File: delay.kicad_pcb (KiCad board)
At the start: 2 copper layers, 0 parts

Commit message: add remaining footprints, start pcb design process
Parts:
- added C1: 10uF, Capacitor:EEE1AA220WR, F.Cu at (89.2, 130.9)
- added C10: 1uF, Capacitor_SMD:C_0805_2012Metric_Pad1.18x1.45mm_HandSolder, F.Cu at (227.4, 80.6)
- added C11: 22nF, Capacitor_SMD:C_0805_2012Metric_Pad1.18x1.45mm_HandSolder, F.Cu at (250.2, 66.2)
- added C12: 2n2, Capacitor_SMD:C_0805_2012Metric_Pad1.18x1.45mm_HandSolder, F.Cu at (232.2, 65.6)
- added C13: 47uF, Capacitor:EEE1AA101SP, F.Cu at (253.5, 74.1)
- added C14: 2n2, Capacitor_SMD:C_0805_2012Metric_Pad1.18x1.45mm_HandSolder, F.Cu at (232.2, 68.6)
- added C15: 47nF, Capacitor_SMD:C_0805_2012Metric_Pad1.18x1.45mm_HandSolder, F.Cu at (232.2, 71.6)
- added C16: 100nF, Capacitor_SMD:C_0805_2012Metric_Pad1.18x1.45mm_HandSolder, F.Cu at (232.2, 74.6)
- added C17: 10nF, Capacitor_SMD:C_0805_2012Metric_Pad1.18x1.45mm_HandSolder, F.Cu at (232.2, 77.6)
- added C18: 15nF, Capacitor_SMD:C_0805_2012Metric_Pad1.18x1.45mm_HandSolder, F.Cu at (232.2, 80.6)
- added C19: 100nF, Capacitor_SMD:C_0805_2012Metric_Pad1.18x1.45mm_HandSolder, F.Cu at (255.3, 66.2)
- added C2: 100uF, Capacitor:EEE1AA101SP, F.Cu at (78.7, 132.1)
- added C20: 1uF, Capacitor_SMD:C_0805_2012Metric_Pad1.18x1.45mm_HandSolder, F.Cu at (237.0, 65.6)
- added C21: 100nF, Capacitor_SMD:C_0805_2012Metric_Pad1.18x1.45mm_HandSolder, F.Cu at (237.0, 68.6)
- added C22: 100nF, Capacitor_SMD:C_0805_2012Metric_Pad1.18x1.45mm_HandSolder, F.Cu at (237.0, 71.6)
- added C23: 1uF, Capacitor_SMD:C_0805_2012Metric_Pad1.18x1.45mm_HandSolder, F.Cu at (237.0, 74.6)
- added C3: 10uF, Capacitor:EEE1AA220WR, F.Cu at (89.2, 138.3)
- added C4: 100nF, Capacitor_SMD:C_0805_2012Metric_Pad1.18x1.45mm_HandSolder, F.Cu at (74.7, 124.5)
- added C5: 1uF, Capacitor_SMD:C_0805_2012Metric_Pad1.18x1.45mm_HandSolder, F.Cu at (161.1, 88.9)
- added C6: 22nF, Capacitor_SMD:C_0805_2012Metric_Pad1.18x1.45mm_HandSolder, F.Cu at (146.0, 86.9)
- added C7: 47pF, Capacitor_SMD:C_0805_2012Metric_Pad1.18x1.45mm_HandSolder, F.Cu at (150.9, 86.8)
- added C8: 100pF, Capacitor_SMD:C_0805_2012Metric_Pad1.18x1.45mm_HandSolder, F.Cu at (163.6, 76.2)
- added C9: 4n7, Capacitor_SMD:C_0805_2012Metric_Pad1.18x1.45mm_HandSolder, F.Cu at (227.4, 77.6)
- added D1: 1N4001, Diodes:DIOM5226X240N, F.Cu at (73.7, 144.8)
- added D2: LED, Diodes:TB00150002BE, F.Cu at (167.6, 132.1)
- added DELAY1: 50kB, Potentiometer_THT:Potentiometer_Alps_RK163_Single_Horizontal, F.Cu at (142.2, 40.6)
- added FDBK1: 50kB, Potentiometer_THT:Potentiometer_Alps_RK163_Single_Horizontal, F.Cu at (167.5, 40.6)
- added J1: Footswitch_Terminal_01x02, Terminal:TB00150002BE, F.Cu at (154.9, 144.8)
- added J2: LED_Socket_01x02, Diodes:TB00150002BE, F.Cu at (167.0, 144.8)
- added J3: Footswitch_Terminal_Signal_01x02, Terminal:TB00150002BE, F.Cu at (180.3, 144.8)
- added J4: Power_Supply_Terminal_01x02, Terminal:TB00150002BE, F.Cu at (210.7, 45.7)
- added J5: IO_Ground_Terminal_01x02, Terminal:TB00150002BE, F.Cu at (226.1, 45.7)
- added MIX1: 50kB, Potentiometer_THT:Potentiometer_Alps_RK163_Single_Horizontal, F.Cu at (192.9, 40.6)
- added R1: 33, Resistor_SMD:R_0805_2012Metric_Pad1.20x1.40mm_HandSolder, F.Cu at (82.3, 121.5)
- added R10: 10k, Resistor_SMD:R_0805_2012Metric_Pad1.20x1.40mm_HandSolder, F.Cu at (189.3, 71.1)
- added R11: 10k, Resistor_SMD:R_0805_2012Metric_Pad1.20x1.40mm_HandSolder, F.Cu at (189.5, 74.7)
- added R12: 5k1, Resistor_SMD:R_0805_2012Metric_Pad1.20x1.40mm_HandSolder, F.Cu at (189.5, 77.6)
- added R13: 10k, Resistor_SMD:R_0805_2012Metric_Pad1.20x1.40mm_HandSolder, F.Cu at (189.5, 80.6)
- added R14: 20k, Resistor_SMD:R_0805_2012Metric_Pad1.20x1.40mm_HandSolder, F.Cu at (189.5, 83.5)
- added R15: 2k7, Resistor_SMD:R_0805_2012Metric_Pad1.20x1.40mm_HandSolder, F.Cu at (199.7, 70.7)
- added R16: 10k, Resistor_SMD:R_0805_2012Metric_Pad1.20x1.40mm_HandSolder, F.Cu at (199.7, 73.7)
- added R17: 1k, Resistor_SMD:R_0805_2012Metric_Pad1.20x1.40mm_HandSolder, F.Cu at (194.0, 71.1)
- added R18: 10k, Resistor_SMD:R_0805_2012Metric_Pad1.20x1.40mm_HandSolder, F.Cu at (194.2, 74.7)
- added R19: 2k, Resistor_SMD:R_0805_2012Metric_Pad1.20x1.40mm_HandSolder, F.Cu at (194.2, 77.6)
- added R2: 10k, Resistor_SMD:R_0805_2012Metric_Pad1.20x1.40mm_HandSolder, F.Cu at (82.3, 124.5)
- added R20: 20k, Resistor_SMD:R_0805_2012Metric_Pad1.20x1.40mm_HandSolder, F.Cu at (163.6, 86.4)
- added R21: 4k7, Resistor_SMD:R_0805_2012Metric_Pad1.20x1.40mm_HandSolder, F.Cu at (166.6, 121.9)
- added R3: 10k, Resistor_SMD:R_0805_2012Metric_Pad1.20x1.40mm_HandSolder, F.Cu at (74.7, 139.7)
- added R4: 1k, Resistor_SMD:R_0805_2012Metric_Pad1.20x1.40mm_HandSolder, F.Cu at (166.6, 88.9)
- added R5: 22k, Resistor_SMD:R_0805_2012Metric_Pad1.20x1.40mm_HandSolder, F.Cu at (161.0, 91.4)
- added R6: 180k, Resistor_SMD:R_0805_2012Metric_Pad1.20x1.40mm_HandSolder, F.Cu at (146.3, 91.4)
- added R7: 1M, Resistor_SMD:R_0805_2012Metric_Pad1.20x1.40mm_HandSolder, F.Cu at (146.3, 94.4)
- added R8: 12k, Resistor_SMD:R_0805_2012Metric_Pad1.20x1.40mm_HandSolder, F.Cu at (163.6, 81.3)
- added R9: 360k, Resistor_SMD:R_0805_2012Metric_Pad1.20x1.40mm_HandSolder, F.Cu at (150.9, 91.4)
- added U1: L7805, Ic:TO255P460X1020X2008-3P, F.Cu at (66.0, 134.6)
- added U2: TL072, Ic:SOT65P280X110-8N, F.Cu at (156.2, 90.5)
- added U3: PT2399, Package_SO:SOIC-16_3.9x9.9mm_P1.27mm, F.Cu at (210.8, 71.1)

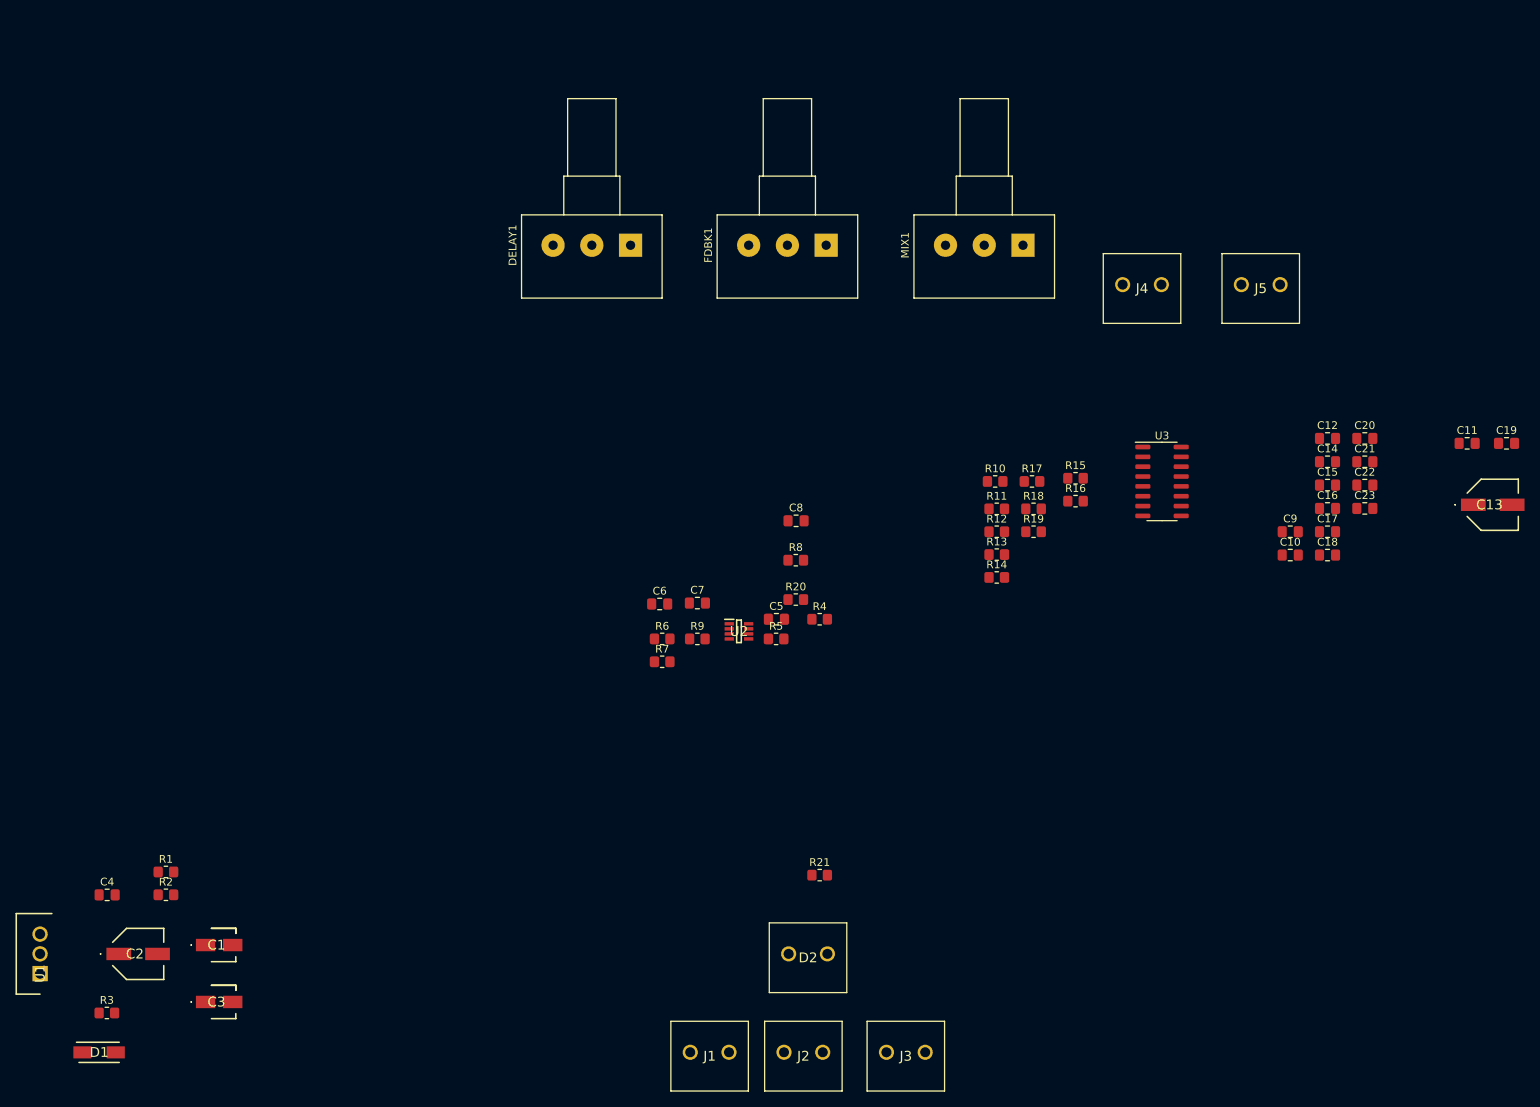
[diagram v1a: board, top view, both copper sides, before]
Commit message: create preliminary pcb spacing design
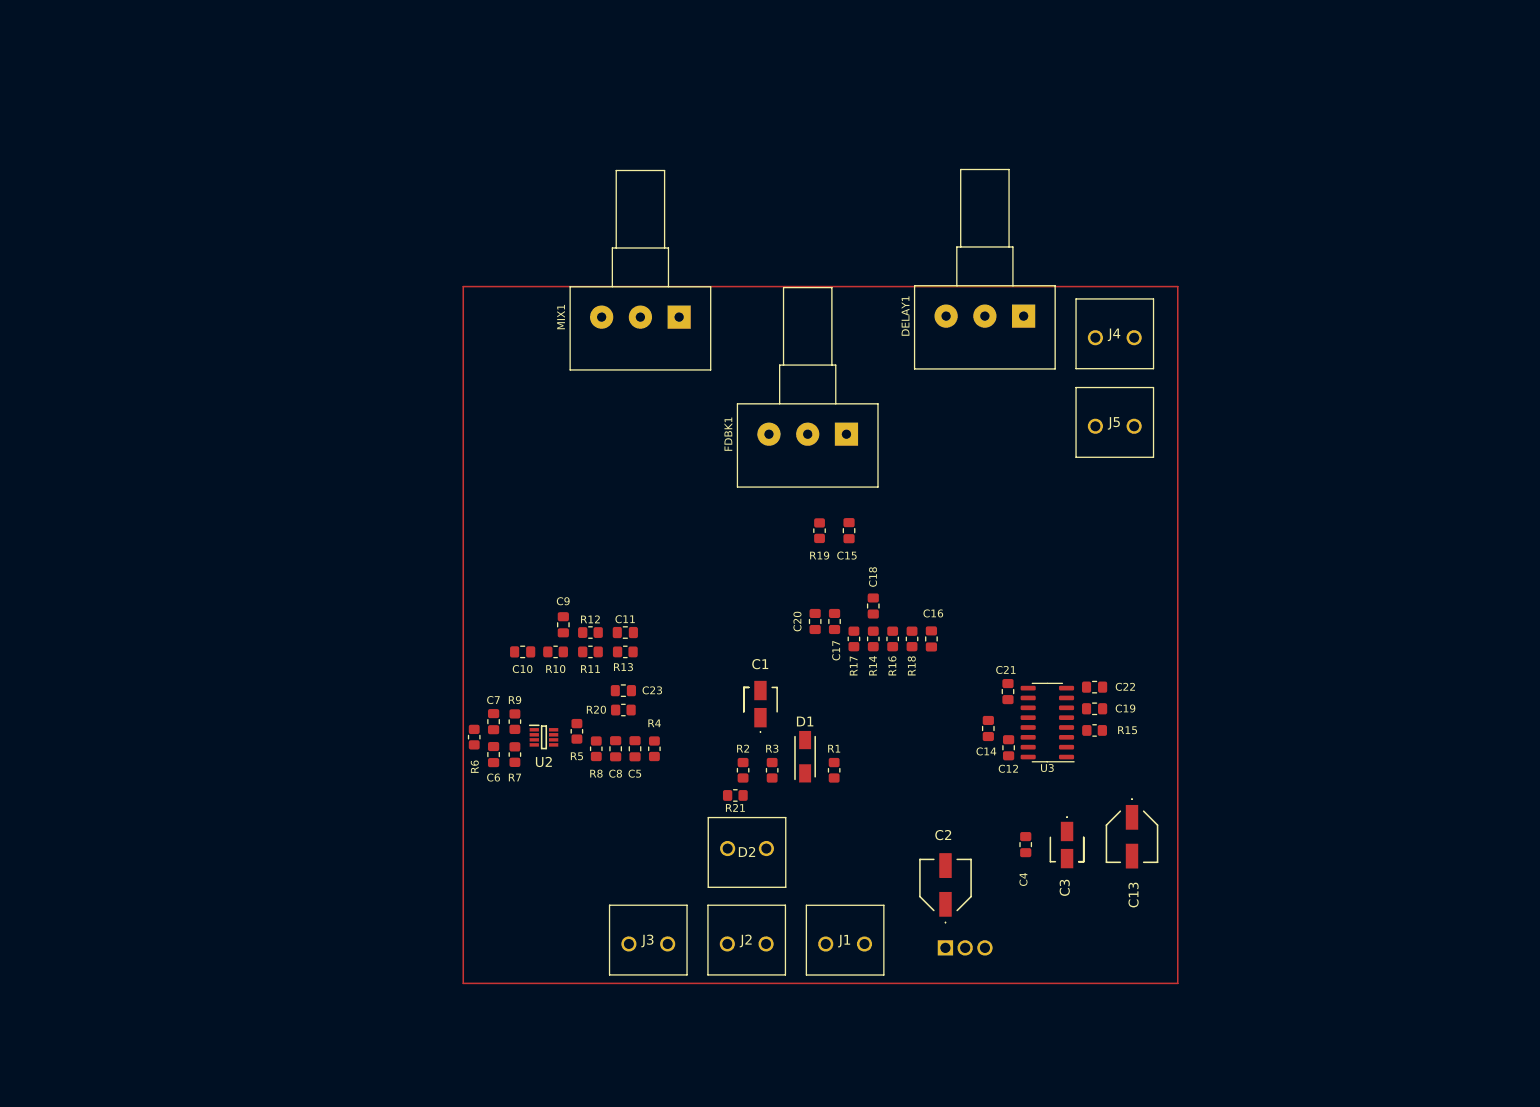
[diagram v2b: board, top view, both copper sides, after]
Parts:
- U1: moved to B.Cu
- moved C4 118.7 mm to (193.2, 118.0), turned to -90 degrees
- moved U1 116.9 mm to (182.9, 131.3), turned to 0 degrees
- moved C11 111.3 mm to (141.6, 90.6)
- moved C3 111.3 mm to (198.6, 118.0), turned to -90 degrees
- moved C2 104.6 mm to (182.9, 123.2), turned to 90 degrees
- moved C10 99.8 mm to (128.3, 93.1), turned to 180 degrees
- moved D1 98.8 mm to (164.8, 106.6), turned to 90 degrees
- moved C23 98.5 mm to (141.3, 98.1)
- moved C9 94.6 mm to (133.6, 89.6), turned to 90 degrees
- moved R3 91.4 mm to (160.5, 108.4), turned to 90 degrees
- moved R1 87.2 mm to (168.5, 108.4), turned to -90 degrees
- moved C1 76.5 mm to (159.0, 99.8), turned to 90 degrees
- moved R2 76.2 mm to (156.8, 108.4), turned to -90 degrees
- moved C20 74.8 mm to (166.1, 89.2), turned to 90 degrees
- moved C17 64.7 mm to (168.6, 89.2), turned to -90 degrees
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
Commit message: add some connections (first draw)
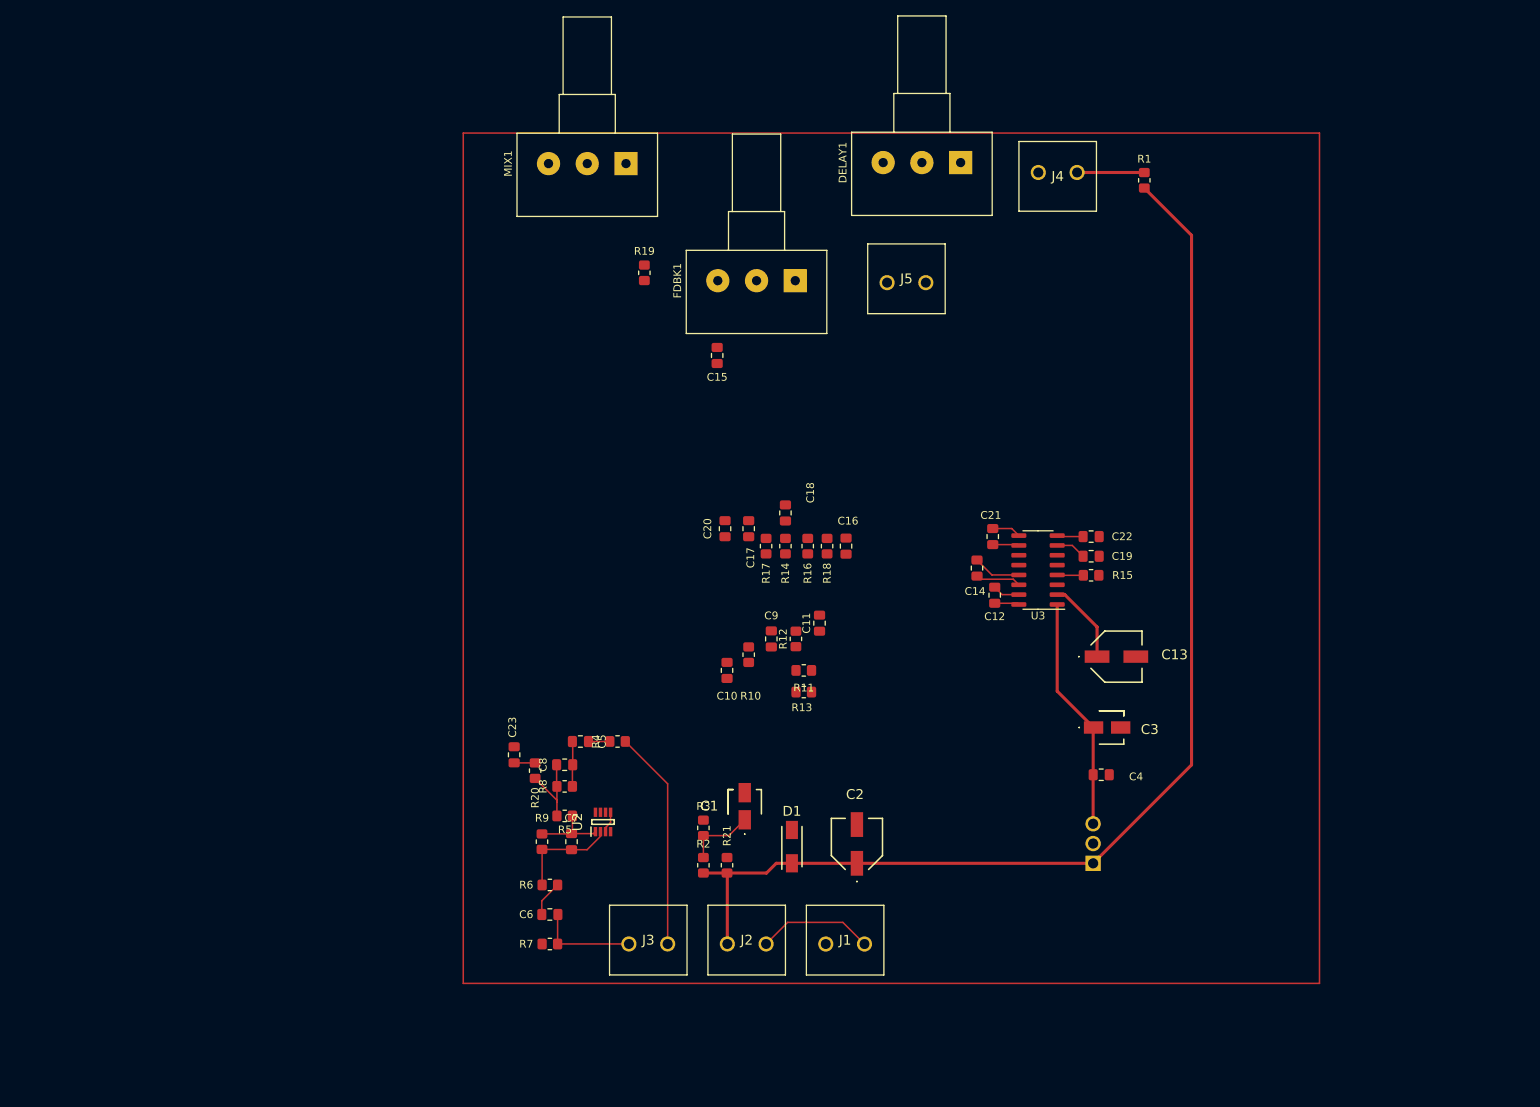
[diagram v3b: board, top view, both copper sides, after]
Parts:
- removed D2: LED, Diodes:TB00150002BE
- moved R1 86.0 mm to (208.5, 32.3)
- moved R19 40.2 mm to (144.0, 44.2)
- moved J5 32.7 mm to (175.3, 45.5)
- moved C15 28.3 mm to (153.4, 54.9), turned to -90 degrees
- moved R11 27.6 mm to (164.6, 95.5)
- moved C9 26.9 mm to (160.4, 91.4)
- moved R12 26.5 mm to (163.6, 91.4), turned to 90 degrees
- moved C10 26.5 mm to (154.7, 95.5), turned to -90 degrees
- moved C11 25.1 mm to (166.6, 89.4), turned to 90 degrees
- moved R10 24.9 mm to (157.5, 93.5), turned to -90 degrees
- moved R7 24.9 mm to (131.8, 130.8), turned to 180 degrees
- moved R13 23.6 mm to (164.6, 98.3)
- moved C13 23.3 mm to (204.9, 93.7), turned to 0 degrees
- moved U1 22.0 mm to (201.9, 120.4), turned to 90 degrees
- moved C6 21.9 mm to (131.8, 127.0), turned to 180 degrees
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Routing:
- net /+LED: track 0.00 -> 155.0 mm
- net /REG_OUT: track 0.00 -> 30.3 mm
- net /OUTPUT: track 0.00 -> 28.4 mm
- net /-LED: track 0.00 -> 15.0 mm
- net Net-(U2A--): track 0.00 -> 13.5 mm
- net /INPUT: track 0.00 -> 13.0 mm
- net /V_B: track 0.00 -> 12.0 mm
- net Net-(U3-REF): track 0.00 -> 10.7 mm
- net Net-(U2B--): track 0.00 -> 10.6 mm
- net /SIGNAL_CLEAN: track 0.00 -> 9.95 mm
- net VDD: track 0.00 -> 8.68 mm
- net Net-(U3-LPF2-IN): track 0.00 -> 6.20 mm
- net Net-(C5-Pad1): track 0.00 -> 5.89 mm
- net Net-(U3-LPF2-OUT): track 0.00 -> 5.86 mm
- net Net-(C6-Pad2): track 0.00 -> 4.65 mm
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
